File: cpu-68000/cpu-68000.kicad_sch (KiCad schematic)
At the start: 14 parts, among them J101 Conn_02x04_Odd_Even, U101 ATF22V10C, U102 ATF22V10C, U103 74HC175, U104 74HC05, X101 10MHz

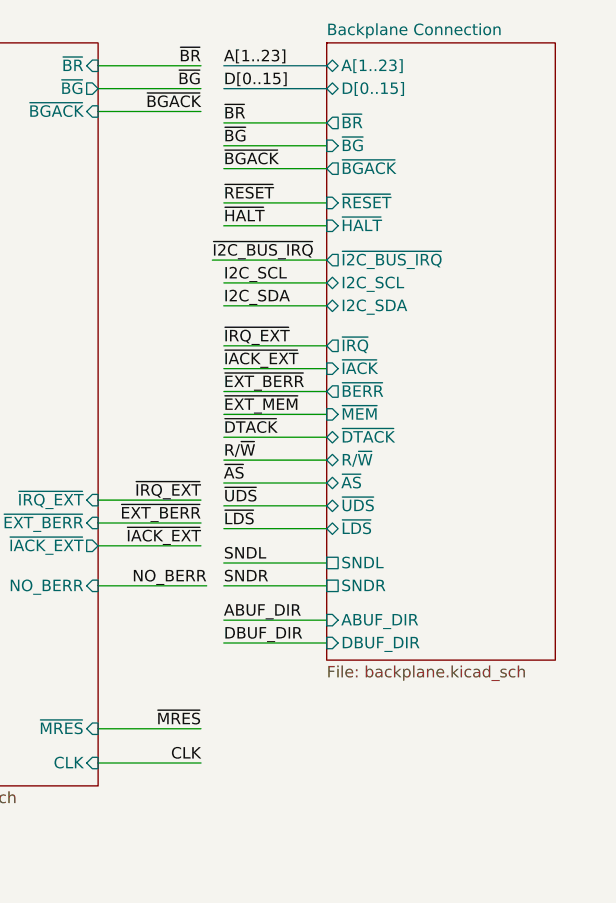
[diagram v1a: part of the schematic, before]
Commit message: Tweaks to IOs on 68k board
- Added an I2C IRQ line, so that I2C peripherals can request servicing.
  This is mostly used for the control panel/backplane management
  functions.
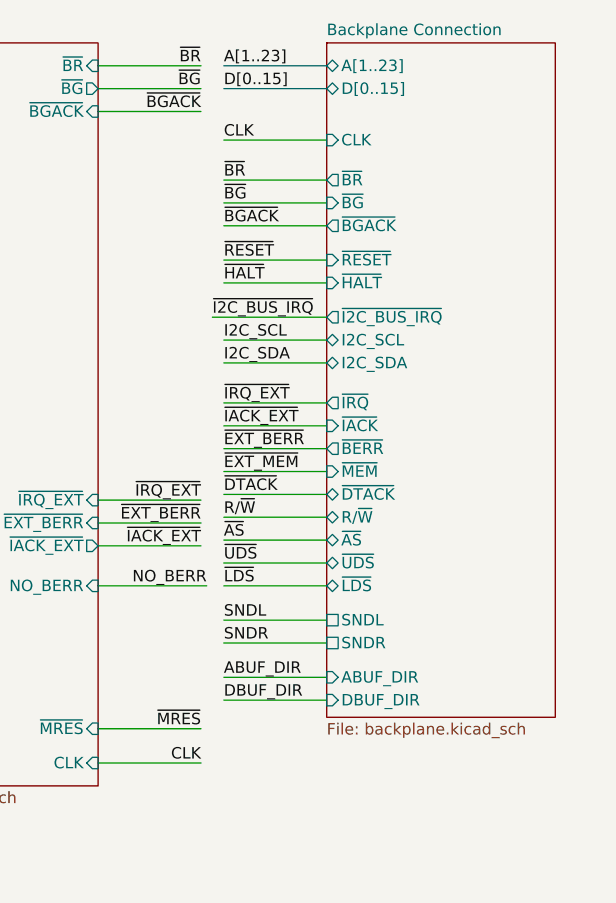
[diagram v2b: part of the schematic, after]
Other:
- sheet Backplane Connection ports: added CLK; removed none

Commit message: Created footprints for PGA 68000
- Also reworked the address decoding for peripherals so all peripherals
  that generate their own /DTACK are on the same half of the peripheral
  address space
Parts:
- X101: MPN (none) -> 1108800
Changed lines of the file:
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@@
-(kicad_sch (version 20210621) (generator eeschema)
+(kicad_sch (version 20211123) (generator eeschema)
   (paper "A4")
-  (junction (at 134.62 153.67) (diameter 0) (color 0 0 0 0))
-  (junction (at 50.8 115.57) (diameter 0) (color 0 0 0 0))
-  (junction (at 134.62 151.13) (diameter 0) (color 0 0 0 0))
-  (junction (at 50.8 120.65) (diameter 0) (color 0 0 0 0))
-  (junction (at 40.64 120.65) (diameter 0) (color 0 0 0 0))
-  (junction (at 116.205 148.59) (diameter 0) (color 0 0 0 0))
-  (junction (at 35.56 188.595) (diameter 0) (color 0 0 0 0))
-  (junction (at 117.475 153.67) (diameter 0) (color 0 0 0 0))
-  (junction (at 114.935 143.51) (diameter 0) (color 0 0 0 0))
-  (junction (at 161.925 138.43) (diameter 0) (color 0 0 0 0))
-  (junction (at 40.64 115.57) (diameter 0) (color 0 0 0 0))
-  (junction (at 35.56 183.515) (diameter 0) (color 0 0 0 0))
-  (junction (at 134.62 156.21) (diameter 0) (color 0 0 0 0))
+  (junction (at 117.475 153.67) (diameter 0) (color 0 0 0 0)
+  )
+  (junction (at 50.8 115.57) (diameter 0) (color 0 0 0 0)
+  )
+  (junction (at 114.935 143.51) (diameter 0) (color 0 0 0 0)
+  )
+  (junction (at 134.62 156.21) (diameter 0) (color 0 0 0 0)
+  )
+  (junction (at 134.62 151.13) (diameter 0) (color 0 0 0 0)
+  )
+  (junction (at 35.56 188.595) (diameter 0) (color 0 0 0 0)
+  )
+  (junction (at 134.62 153.67) (diameter 0) (color 0 0 0 0)
+  )
+  (junction (at 116.205 148.59) (diameter 0) (color 0 0 0 0)
+  )
+  (junction (at 35.56 183.515) (diameter 0) (color 0 0 0 0)
+  )
+  (junction (at 40.64 115.57) (diameter 0) (color 0 0 0 0)
+  )
+  (junction (at 161.925 138.43) (diameter 0) (color 0 0 0 0)
+  )
+  (junction (at 50.8 120.65) (diameter 0) (color 0 0 0 0)
+  )
+  (junction (at 40.64 120.65) (diameter 0) (color 0 0 0 0)
+  )
   (wire (pts (xy 55.88 95.885) (xy 67.945 95.885))
     (stroke (width 0) (type default) (color 0 0 0 0))
@@
       (effects (font (size 1.27 1.27)) hide)
     )
+    (property "MPN" "1108800" (id 4) (at 260.35 150.495 0)
+      (effects (font (size 1.27 1.27)) hide)
+    )
     (pin "1")
     (pin "4")
@@
       (reference "#PWR0175") (unit 1) (value "GND") (footprint "")
     )
-    (path "/d78c8e5b-f415-45d2-97bd-68d83365a2b9/6f5e6568-5e17-4385-8282-358986ef60df"
-      (reference "#PWR0176") (unit 1) (value "+5V") (footprint "")
-    )
     (path "/dd09b3c7-f3f1-4702-9c67-cfc029c2d128/3f1391f1-ee3b-4398-bbe1-41adbe6c7891"
       (reference "#PWR0177") (unit 1) (value "GND") (footprint "")
     )
-    (path "/d78c8e5b-f415-45d2-97bd-68d83365a2b9/ea58146b-5399-4d23-9386-509363cb78ef"
-      (reference "#PWR0178") (unit 1) (value "GND") (footprint "")
-    )
     (path "/d78c8e5b-f415-45d2-97bd-68d83365a2b9/ff55bbc5-72fd-455f-b717-f01358e2d4be"
       (reference "#PWR0179") (unit 1) (value "+5V") (footprint "")
@@
       (reference "#PWR0625") (unit 1) (value "GND") (footprint "")
     )
+    (path "/d78c8e5b-f415-45d2-97bd-68d83365a2b9/5d841968-d13a-47b4-862e-419d30a5db47"
+      (reference "#PWR?") (unit 1) (value "GND") (footprint "")
+    )
+    (path "/d78c8e5b-f415-45d2-97bd-68d83365a2b9/b4ecea00-1db5-44fe-9fe0-3b6f531d359b"
+      (reference "#PWR?") (unit 1) (value "+5V") (footprint "")
+    )
     (path "/663fdf24-72f5-4662-98d1-8ad3c280cd08"
       (reference "C101") (unit 1) (value "4.7µF") (footprint "Capacitor_SMD:C_0805_2012Metric")
@@
     )
     (path "/d78c8e5b-f415-45d2-97bd-68d83365a2b9/62adabf5-8f35-4e69-8692-db2cbe767550"
-      (reference "U301") (unit 1) (value "MC68000FN") (footprint "Package_LCC:PLCC-68_THT-Socket")
+      (reference "U301") (unit 1) (value "MC68000R") (footprint "68komputer-common:PGA-68-10x10")
     )
     (path "/d78c8e5b-f415-45d2-97bd-68d83365a2b9/7663401e-9484-42d0-b9ad-ce98c893a7cb"

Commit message: Added high byte flash chip
- Replaced one of the RAMs with another flash, so that we can have
  on-board boot ROM of 1M. It'll have to be programmed in system (or
  very flimsily out of system before soldering) so a switch to remap the
  flash to elsehwere in the address space is provided (formerly BERR
  inhibit switch)
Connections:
- net ROM_REMAP: now reaches U102.11 (IN11)
- net ~{RAM1_CS} renamed ~{RAM_CS}
- net ~{RAM2_CS} renamed ~{ROM_CS}
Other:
- sheet Main CPU ports: added none; removed NO_BERR
- sheet Memory ports: added ~{RAM_CS}, ~{ROM_CS}; removed ~{RAM1_CS}, ~{RAM2_CS}
- sheet Peripherals ports: added REMAP; removed NO_BERR
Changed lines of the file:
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@@
+    (stroke (width 0) (type default) (color 0 0 0 0))
+  )
+  (wire (pts (xy 23.495 163.83) (xy 35.56 163.83))
     (stroke (width 0) (type default) (color 0 0 0 0))
   )
@@
   )
   (wire (pts (xy 161.925 138.43) (xy 172.085 138.43))
-    (stroke (width 0) (type default) (color 0 0 0 0))
-  )
-  (wire (pts (xy 240.665 79.375) (xy 228.6 79.375))
     (stroke (width 0) (type default) (color 0 0 0 0))
   )
@@
     (effects (font (size 1.27 1.27)) (justify left bottom))
   )
+  (label "ROM_REMAP" (at 23.495 163.83 0)
+    (effects (font (size 1.27 1.27)) (justify left bottom))
+  )
   (label "~{MRES}" (at 240.03 95.25 180)
     (effects (font (size 1.27 1.27)) (justify right bottom))
@@
     (effects (font (size 1.27 1.27)) (justify left bottom))
   )
-  (label "NO_BERR" (at 240.665 79.375 180)
-    (effects (font (size 1.27 1.27)) (justify right bottom))
-  )
   (label "I2C_SCL" (at 139.065 21.59 180)
     (effects (font (size 1.27 1.27)) (justify right bottom))
   )
-  (label "~{RAM2_CS}" (at 67.945 143.51 180)
+  (label "~{ROM_CS}" (at 67.945 143.51 180)
     (effects (font (size 1.27 1.27)) (justify right bottom))
   )
@@
     (effects (font (size 1.27 1.27)) (justify left bottom))
   )
-  (label "~{RAM2_CS}" (at 140.335 79.375 0)
+  (label "~{ROM_CS}" (at 140.335 79.375 0)
     (effects (font (size 1.27 1.27)) (justify left bottom))
   )
@@
     (effects (font (size 1.27 1.27)) (justify left bottom))
   )
-  (label "~{RAM1_CS}" (at 140.335 76.835 0)
+  (label "~{RAM_CS}" (at 140.335 76.835 0)
     (effects (font (size 1.27 1.27)) (justify left bottom))
   )
@@
     (effects (font (size 1.27 1.27)) (justify left bottom))
   )
-  (label "NO_BERR" (at 89.535 25.4 0)
+  (label "ROM_REMAP" (at 89.535 25.4 0)
     (effects (font (size 1.27 1.27)) (justify left bottom))
   )
@@
     (effects (font (size 1.27 1.27)) (justify left bottom))
   )
-  (label "~{RAM1_CS}" (at 67.945 146.05 180)
+  (label "~{RAM_CS}" (at 67.945 146.05 180)
     (effects (font (size 1.27 1.27)) (justify right bottom))
   )
@@
       (effects (font (size 1.27 1.27)) (justify left))
     )
-    (pin "NO_BERR" output (at 101.6 25.4 180)
+    (pin "REMAP" output (at 101.6 25.4 180)
       (effects (font (size 1.27 1.27)) (justify left))
     )
@@
       (effects (font (size 1.27 1.27)) (justify left))
     )
-    (pin "NO_BERR" input (at 228.6 79.375 0)
-      (effects (font (size 1.27 1.27)) (justify right))
-    )
     (pin "~{HALT}" bidirectional (at 203.2 24.13 180)
       (effects (font (size 1.27 1.27)) (justify left))
@@
       (effects (font (size 1.27 1.27)) (justify left))
     )
-    (pin "~{RAM1_CS}" input (at 152.4 76.835 180)
-      (effects (font (size 1.27 1.27)) (justify left))
-    )
-    (pin "~{RAM2_CS}" input (at 152.4 79.375 180)
+    (pin "~{RAM_CS}" input (at 152.4 76.835 180)
+      (effects (font (size 1.27 1.27)) (justify left))
+    )
+    (pin "~{ROM_CS}" input (at 152.4 79.375 180)
       (effects (font (size 1.27 1.27)) (justify left))
     )
@@
       (reference "C406") (unit 1) (value "4.7µF") (footprint "Capacitor_SMD:C_0805_2012Metric")
     )
+    (path "/de637fe6-6976-492c-a9e4-b196304c5ff6/a52e5a4a-ff61-4952-9a10-e35cfdaf789b"
+      (reference "C407") (unit 1) (value "100nF") (footprint "Capacitor_SMD:C_0805_2012Metric")
+    )
     (path "/de637fe6-6976-492c-a9e4-b196304c5ff6/b6f6b9a9-1591-42cf-a0fe-74e325fe224f"
       (reference "C408") (unit 1) (value "100nF") (footprint "Capacitor_SMD:C_0805_2012Metric")
     )
+    (path "/de637fe6-6976-492c-a9e4-b196304c5ff6/c26884fa-57ac-4619-8f87-0f4d186a9e52"
+      (reference "C409") (unit 1) (value "100nF") (footprint "Capacitor_SMD:C_0805_2012Metric")
+    )
     (path "/de637fe6-6976-492c-a9e4-b196304c5ff6/805d9049-c276-4b92-b73f-00317838ddc7"
       (reference "C410") (unit 1) (value "100nF") (footprint "Capacitor_SMD:C_0805_2012Metric")
@@
       (reference "U401") (unit 1) (value "SST39SF040-XX-4X-W") (footprint "Package_SO:TSOP-I-32_11.8x8mm_P0.5mm")
     )
-    (path "/de637fe6-6976-492c-a9e4-b196304c5ff6/b607f902-c234-4629-8816-d2d0d79eb9bb"
-      (reference "U402") (unit 1) (value "IS61C5128AL-10TLI") (footprint "Package_SO:TSOP-II-44_10.16x18.41mm_P0.8mm")
+    (path "/de637fe6-6976-492c-a9e4-b196304c5ff6/a35c7cd1-2b1c-43c6-8464-c04abae1d122"
+      (reference "U402") (unit 1) (value "SST39SF040-XX-4X-W") (footprint "Package_SO:TSOP-I-32_11.8x8mm_P0.5mm")
     )
     (path "/de637fe6-6976-492c-a9e4-b196304c5ff6/102c0762-bf26-4ed5-a23d-36e3a9224e60"

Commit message: Reworked /BERR behavior
- The /BERR line on the backplane connector is now the same that is
  going to the CPU; this means that external devices can detect when
  they access unmapped space when /BERR is asserted during bus mastering
  operation.

  Spare gate of open drain inverter was used to convert the active high
  bus error timeout to assert /BERR.
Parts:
- removed unit 1 of U104
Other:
- sheet Main CPU ports: added ~{BERR}; removed ~{EXT_BERR}
- note removed: "Spare"
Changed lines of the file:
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@@
-    (stroke (width 0) (type default) (color 0 0 0 0))
-  )
-  (wire (pts (xy 193.04 138.43) (xy 193.04 151.13))
     (stroke (width 0) (type default) (color 0 0 0 0))
   )
@@
     (effects (font (size 1.27 1.27)) (justify left bottom))
   )
-  (text "Spare" (at 198.12 128.27 0)
-    (effects (font (size 1.27 1.27) italic) (justify left bottom))
-  )
   (text "Misc Glue Logic" (at 38.1 64.77 0)
     (effects (font (size 1.27 1.27) italic) (justify left bottom))
@@
     (effects (font (size 1.27 1.27)) (justify left bottom))
   )
-  (label "~{EXT_BERR}" (at 240.03 72.39 180)
+  (label "~{BERR}" (at 240.03 72.39 180)
     (effects (font (size 1.27 1.27)) (justify right bottom))
   )
@@
     (effects (font (size 1.27 1.27)) (justify left bottom))
   )
-  (label "~{EXT_BERR}" (at 242.57 64.135 0)
+  (label "~{BERR}" (at 242.57 64.135 0)
     (effects (font (size 1.27 1.27)) (justify left bottom))
   )
@@
     (pin "2")
   )
-  (symbol (lib_id "power:GND") (at 193.04 151.13 0) (unit 1)
-    (in_bom yes) (on_board yes) (fields_autoplaced)
-    (property "Reference" "#PWR0142" (id 0) (at 193.04 157.48 0)
-      (effects (font (size 1.27 1.27)) hide)
-    )
-    (property "Value" "GND" (id 1) (at 193.04 155.6924 0))
-    (property "Footprint" "" (id 2) (at 193.04 151.13 0)
-      (effects (font (size 1.27 1.27)) hide)
-    )
-    (property "Datasheet" "" (id 3) (at 193.04 151.13 0)
-      (effects (font (size 1.27 1.27)) hide)
-    )
-    (pin "1")
-  )
   (symbol (lib_id "power:+5V") (at 35.56 171.45 90) (unit 1)
     (in_bom yes) (on_board yes) (fields_autoplaced)
@@
     )
     (pin "1")
-  )
-  (symbol (lib_id "74xx:74LS05") (at 200.66 138.43 0) (unit 1)
-    (in_bom yes) (on_board yes) (fields_autoplaced)
-    (property "Reference" "U104" (id 0) (at 200.66 130.6535 0))
-    (property "Value" "74HC05" (id 1) (at 200.66 133.4286 0))
-    (property "Footprint" "Package_SO:SOIC-14_3.9x8.7mm_P1.27mm" (id 2) (at 200.66 138.43 0)
-      (effects (font (size 1.27 1.27)) hide)
-    )
-    (property "Datasheet" "http://www.ti.com/lit/gpn/sn74LS05" (id 3) (at 200.66 138.43 0)
-      (effects (font (size 1.27 1.27)) hide)
-    )
-    (pin "1")
-    (pin "2")
   )
   (symbol (lib_id "power:GND") (at 139.7 177.165 0) (unit 1)
@@
       (effects (font (size 1.27 1.27)) (justify right))
     )
-    (pin "~{EXT_BERR}" input (at 228.6 72.39 0)
+    (pin "~{BERR}" input (at 228.6 72.39 0)
       (effects (font (size 1.27 1.27)) (justify right))
     )
@@
       (reference "#PWR0141") (unit 1) (value "GND") (footprint "")
     )
-    (path "/12304412-a0bc-47ae-ba8c-e7e805495f59"
-      (reference "#PWR0142") (unit 1) (value "GND") (footprint "")
-    )
     (path "/a80fdcbe-0bb0-435d-8e84-e8399e2a8c71/b56470d6-5960-4d62-9665-9bfc99b9f0da"
       (reference "#PWR0143") (unit 1) (value "GND") (footprint "")
@@
       (reference "U103") (unit 1) (value "74HC175") (footprint "Package_SO:TSSOP-16_4.4x5mm_P0.65mm")
     )
-    (path "/2fea9f65-bf0a-45b4-b894-2125d907b942"
+    (path "/d78c8e5b-f415-45d2-97bd-68d83365a2b9/5f5d970f-b845-4d3d-b073-2fe6c72aae11"
       (reference "U104") (unit 1) (value "74HC05") (footprint "Package_SO:SOIC-14_3.9x8.7mm_P1.27mm")
     )

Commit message: Expose CPU function code on backplane
- Routed the function code signals to the backplane; they're pulled to
  ground so that if a bus mastering device doesn't drive them the world
  won't explode (it will be a supervisor data access)
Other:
- sheet Backplane Connection ports: added FC[0..2]; removed none
- sheet Main CPU ports: added FC[0..2]; removed none
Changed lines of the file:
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@@
+    (stroke (width 0) (type default) (color 0 0 0 0))
+  )
+  (bus (pts (xy 191.77 49.53) (xy 203.2 49.53))
     (stroke (width 0) (type default) (color 0 0 0 0))
   )
@@
   )
   (wire (pts (xy 152.4 73.025) (xy 140.335 73.025))
+    (stroke (width 0) (type default) (color 0 0 0 0))
+  )
+  (bus (pts (xy 242.57 26.67) (xy 254 26.67))
     (stroke (width 0) (type default) (color 0 0 0 0))
   )
@@
     (effects (font (size 1.27 1.27)) (justify left bottom))
   )
+  (label "FC[0..2]" (at 242.57 26.67 0)
+    (effects (font (size 1.27 1.27)) (justify left bottom))
+  )
   (label "D[0..15]" (at 191.77 46.99 0)
     (effects (font (size 1.27 1.27)) (justify left bottom))
@@
   )
   (label "~{PERIPH}" (at 89.535 80.645 0)
+    (effects (font (size 1.27 1.27)) (justify left bottom))
+  )
+  (label "FC[0..2]" (at 191.77 49.53 0)
     (effects (font (size 1.27 1.27)) (justify left bottom))
   )
@@
       (effects (font (size 1.27 1.27)) (justify left))
     )
+    (pin "FC[0..2]" output (at 203.2 49.53 180)
+      (effects (font (size 1.27 1.27)) (justify left))
+    )
   )
   (sheet (at 254 19.05) (size 25.4 74.93) (fields_autoplaced)
@@
       (effects (font (size 1.27 1.27)) (justify left))
     )
+    (pin "FC[0..2]" bidirectional (at 254 26.67 180)
+      (effects (font (size 1.27 1.27)) (justify left))
+    )
